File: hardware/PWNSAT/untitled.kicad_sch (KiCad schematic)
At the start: 54 parts, among them J1 Conn_01x03, J2 Conn_01x04_Pin, SW1 SW_Push, SW2 SW_Push, U2 W25N02KVZEIR, Y1 Crystal, Y2 24MHz

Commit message: feat(Hw):Update_Battery_Sch_And_Sensors_And_PWNCube
pending_Outputs_connectors
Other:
- company: (none) -> ElectronicCats
- title: (none) -> PWNCube
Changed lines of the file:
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@@
 	(generator_version "9.0")
 	(paper "A3")
+	(title_block
+		(title "PWNCube")
+		(date "2026-01-23")
+		(rev "1.0")
+		(company "ElectronicCats")
+		(comment 1 "Edgar Capuchino")
+	)
 	(text "FLASH\n"
 		(exclude_from_sim no)

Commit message: feat(Hw):floorplans_updated
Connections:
- net R1_SCK: now reaches U1.38 (EMMC_D5/SPI1_CLK_M0/UART1_RX_M2/I2C2_SCL_M1/GPIO4__A7_U)
- net R1_NSS: now reaches U1.40 (EMMC_D4/SPI1_CS0_M0/UART1_TX_M2/I2C2_SDA_M1/GPIO4__A5_U)
- net R1_MOSI: now reaches U1.45 (EMMC_D6/SPI1_MOSI_M0/UART0_TX_M2/I2C0_SCL_M1/GPIO_4_A1_U)
- net R1_MISO: now reaches U1.46 (EMMC_D7/SPI1_MISO_M0/UART0_RX_M2/I2C0_SDA_M1/GPIO_4_A0_U)
- net R1_RST: now reaches U1.83 (VO_LCDC_D1/VI_CIF_D8_M1/PWM10_M1/UART4_RTS__M1/GPIO1_C6_D)
- net R1_BUSY: now reaches U1.84 (VO_LCDC_D0/VI_CIF_D9_M1/PWM11_IR_M1/UART4_CT_S_M1/GPIO1_C7_D)
- net R1_DIO3: now reaches U1.85 (VO_LCDC_CLK/VI_CIF_CLKO_M1/I2C3_SCL_M1/UART5__TX_M1/PWM11_IR_M2/AUD_DSM_N/GPIO1_D3_D)
- net R1_DIO2: now reaches U1.86 (VO_LCDC_VSYNC/VI_CIF_VSYNC_M1/I2C3_SDA_M1/UA_RT5_RX_M1/SPI0_CS1_M0/PWM0_M1/AUD_DSM_P/GPI_O1_D2_D)
- net R1_DIO1: now reaches U1.87 (VO_LCDC_HSYNC/VI_CIF_HREF_M1/PWM10_M2/UART5__CTS_M1/UART3_RX_M1/GPIO1_D1_D)
- net DIO23: now reaches U1.89 (VO_LCDC_DEN/VI_CIF_CLKI_M1/PWM3_IR_M2/UART5__RTS_M1/UART3_TX_M1/GPIO1_D0_D)
- net R1_ANT_SW: now reaches U1.90 (VO_LCDC_D2/VI_CIF_D7_M1/PWM9_M1/UART4_TX_M1/_SDMMC1_D2_M1/GPIO1_C5_D)
- no-connect marks 56 -> 45
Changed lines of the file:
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@@
 	)
 	(no_connect
-		(at 283.21 88.9)
-	)
-	(no_connect
 		(at 287.02 177.8)
 	)
@@
 	)
 	(no_connect
-		(at 283.21 81.28)
-	)
-	(no_connect
 		(at 144.78 127)
 	)
 	(no_connect
-		(at 144.78 142.24)
-	)
-	(no_connect
 		(at 287.02 195.58)
 	)
@@
 	)
 	(no_connect
-		(at 144.78 137.16)
-	)
-	(no_connect
 		(at 287.02 147.32)
 	)
@@
 	)
 	(no_connect
-		(at 283.21 91.44)
-	)
-	(no_connect
 		(at 287.02 142.24)
 	)
@@
 	)
 	(no_connect
-		(at 283.21 83.82)
-	)
-	(no_connect
 		(at 134.62 39.37)
 	)
@@
 	)
 	(no_connect
-		(at 144.78 157.48)
-	)
-	(no_connect
 		(at 287.02 154.94)
 	)
@@
 	)
 	(no_connect
-		(at 283.21 76.2)
-	)
-	(no_connect
 		(at 134.62 95.25)
 	)
@@
 	)
 	(no_connect
-		(at 283.21 73.66)
-	)
-	(no_connect
-		(at 283.21 78.74)
-	)
-	(no_connect
 		(at 283.21 58.42)
 	)
@@
 	)
 	(no_connect
-		(at 144.78 154.94)
-	)
-	(no_connect
 		(at 287.02 165.1)
 	)
@@
 	(wire
 		(pts
+			(xy 271.78 81.28) (xy 283.21 81.28)
+		)
+		(stroke
+			(width 0)
+			(type default)
+		)
+	)
+	(wire
+		(pts
 			(xy 214.63 256.54) (xy 212.09 256.54)
 		)
@@
 	(wire
 		(pts
-			(xy 127 134.62) (xy 144.78 134.62)
+			(xy 120.65 134.62) (xy 144.78 134.62)
 		)
 		(stroke
@@
 	(wire
 		(pts
+			(xy 271.78 91.44) (xy 283.21 91.44)
+		)
+		(stroke
+			(width 0)
+			(type default)
+		)
+	)
+	(wire
+		(pts
 			(xy 57.15 80.01) (xy 57.15 82.55)
 		)
@@
 	(wire
 		(pts
-			(xy 127 138.43) (xy 127 134.62)
+			(xy 120.65 137.16) (xy 120.65 134.62)
 		)
 		(stroke
@@
 	(wire
 		(pts
+			(xy 271.78 83.82) (xy 283.21 83.82)
+		)
+		(stroke
+			(width 0)
+			(type default)
+		)
+	)
+	(wire
+		(pts
 			(xy 74.93 82.55) (xy 74.93 80.01)
 		)
@@
 	(wire
 		(pts
+			(xy 129.54 154.94) (xy 144.78 154.94)
+		)
+		(stroke
+			(width 0)
+			(type default)
+		)
+	)
+	(wire
+		(pts
 			(xy 44.45 54.61) (xy 44.45 58.42)
 		)
@@
 	(wire
 		(pts
+			(xy 129.54 157.48) (xy 144.78 157.48)
+		)
+		(stroke
+			(width 0)
+			(type default)
+		)
+	)
+	(wire
+		(pts
 			(xy 50.8 71.12) (xy 50.8 73.66)
 		)
@@
 	(wire
 		(pts
+			(xy 271.78 76.2) (xy 283.21 76.2)
+		)
+		(stroke
+			(width 0)
+			(type default)
+		)
+	)
+	(wire
+		(pts
 			(xy 274.32 162.56) (xy 287.02 162.56)
 		)
@@
 	(wire
 		(pts
+			(xy 129.54 137.16) (xy 144.78 137.16)
+		)
+		(stroke
+			(width 0)
+			(type default)
+		)
+	)
+	(wire
+		(pts
+			(xy 271.78 88.9) (xy 283.21 88.9)
+		)
+		(stroke
+			(width 0)
+			(type default)
+		)
+	)
+	(wire
+		(pts
 			(xy 248.92 271.78) (xy 238.76 271.78)
 		)
@@
 	(wire
 		(pts
+			(xy 271.78 78.74) (xy 283.21 78.74)
+		)
+		(stroke
+			(width 0)
+			(type default)
+		)
+	)
+	(wire
+		(pts
 			(xy 33.02 110.49) (xy 33.02 113.03)
 		)
@@
 	(wire
 		(pts
+			(xy 271.78 73.66) (xy 283.21 73.66)
+		)
+		(stroke
+			(width 0)
+			(type default)
+		)
+	)
+	(wire
+		(pts
 			(xy 119.38 80.01) (xy 134.62 80.01)
 		)
@@
 	(wire
 		(pts
+			(xy 129.54 142.24) (xy 144.78 142.24)
+		)
+		(stroke
+			(width 0)
+			(type default)
+		)
+	)
+	(wire
+		(pts
 			(xy 22.86 100.33) (xy 24.13 100.33)
 		)
@@
 		)
 	)
+	(hierarchical_label "R1_BUSY"
+		(shape input)
+		(at 271.78 76.2 180)
+		(effects
+			(font
+				(size 1.27 1.27)
+			)
+			(justify right)
+		)
+	)
 	(hierarchical_label "DIO2"
 		(shape input)
@@
 		)
 	)
+	(hierarchical_label "R1_MOSI"
+		(shape input)
+		(at 129.54 154.94 180)
+		(effects
+			(font
+				(size 1.27 1.27)
+			)
+			(justify right)
+		)
+	)
 	(hierarchical_label "INT2"
 		(shape output)
@@
 		)
 	)
+	(hierarchical_label "R1_ANT_SW"
+		(shape input)
+		(at 271.78 91.44 180)
+		(effects
+			(font
+				(size 1.27 1.27)
+			)
+			(justify right)
+		)
+	)
 	(hierarchical_label "R0_MOSI"
 		(shape input)
@@
 		)
 	)
+	(hierarchical_label "R1_DIO3"
+		(shape input)
+		(at 271.78 78.74 180)
+		(effects
+			(font
+				(size 1.27 1.27)
+			)
+			(justify right)
+		)
+	)
 	(hierarchical_label "v_0.9v"
 		(shape input)
@@
 		)
 	)
+	(hierarchical_label "R1_NSS"
+		(shape input)
+		(at 129.54 142.24 180)
+		(effects
+			(font
+				(size 1.27 1.27)
+			)
+			(justify right)
+		)
+	)
 	(hierarchical_label "v_0.9v"
 		(shape input)
@@
 		)
 	)
+	(hierarchical_label "R1_MISO"
+		(shape input)
+		(at 129.54 157.48 180)
+		(effects
+			(font
+				(size 1.27 1.27)
+			)
+			(justify right)
+		)
+	)
 	(hierarchical_label "v_3v3"
 		(shape input)
@@
 		)
 	)
+	(hierarchical_label "R1_DIO2"
+		(shape input)
+		(at 271.78 81.28 180)
+		(effects
+			(font
+				(size 1.27 1.27)
+			)
+			(justify right)
+		)
+	)
 	(hierarchical_label "INT1"
 		(shape output)
@@
 		)
 	)
+	(hierarchical_label "R1_DIO1"
+		(shape input)
+		(at 271.78 83.82 180)
+		(effects
+			(font
+				(size 1.27 1.27)
+			)
+			(justify right)
+		)
+	)
 	(hierarchical_label "VCC_DDR"
 		(shape input)
@@
 		)
 	)
+	(hierarchical_label "R1_SCK"
+		(shape input)
+		(at 129.54 137.16 180)
+		(effects
+			(font
+				(size 1.27 1.27)
+			)
+			(justify right)
+		)
+	)
 	(hierarchical_label "v_0.9v"
 		(shape input)
@@
 		)
 	)
+	(hierarchical_label "R1_RST"
+		(shape input)
+		(at 271.78 73.66 180)
+		(effects
+			(font
+				(size 1.27 1.27)
+			)
+			(justify right)
+		)
+	)
 	(hierarchical_label "v_3v3"
 		(shape input)
@@
 		)
 	)
+	(hierarchical_label "DIO23"
+		(shape input)
+		(at 271.78 88.9 180)
+		(effects
+			(font
+				(size 1.27 1.27)
+			)
+			(justify right)
+		)
+	)
 	(hierarchical_label "v_1.8v"
 		(shape input)
@@
 	(symbol
 		(lib_id "power:GND")
-		(at 127 138.43 0)
+		(at 120.65 137.16 0)
 		(unit 1)
 		(exclude_from_sim no)
@@
 		(dnp no)
 		(property "Reference" "#PWR016"
-			(at 127 144.78 0)
+			(at 120.65 143.51 0)
 			(effects
 				(font
@@
 		)
 		(property "Value" "GND"
-			(at 123.952 138.684 0)
+			(at 117.602 137.414 0)
 			(effects
 				(font
@@
 		)
 		(property "Footprint" ""
-			(at 127 138.43 0)
+			(at 120.65 137.16 0)
 			(effects
 				(font
@@
 		)
 		(property "Datasheet" ""
-			(at 127 138.43 0)
+			(at 120.65 137.16 0)
 			(effects
 				(font
@@
 		)
 		(property "Description" "Power symbol creates a global label with name \"GND\" , ground"
-			(at 127 138.43 0)
+			(at 120.65 137.16 0)
 			(effects
 				(font

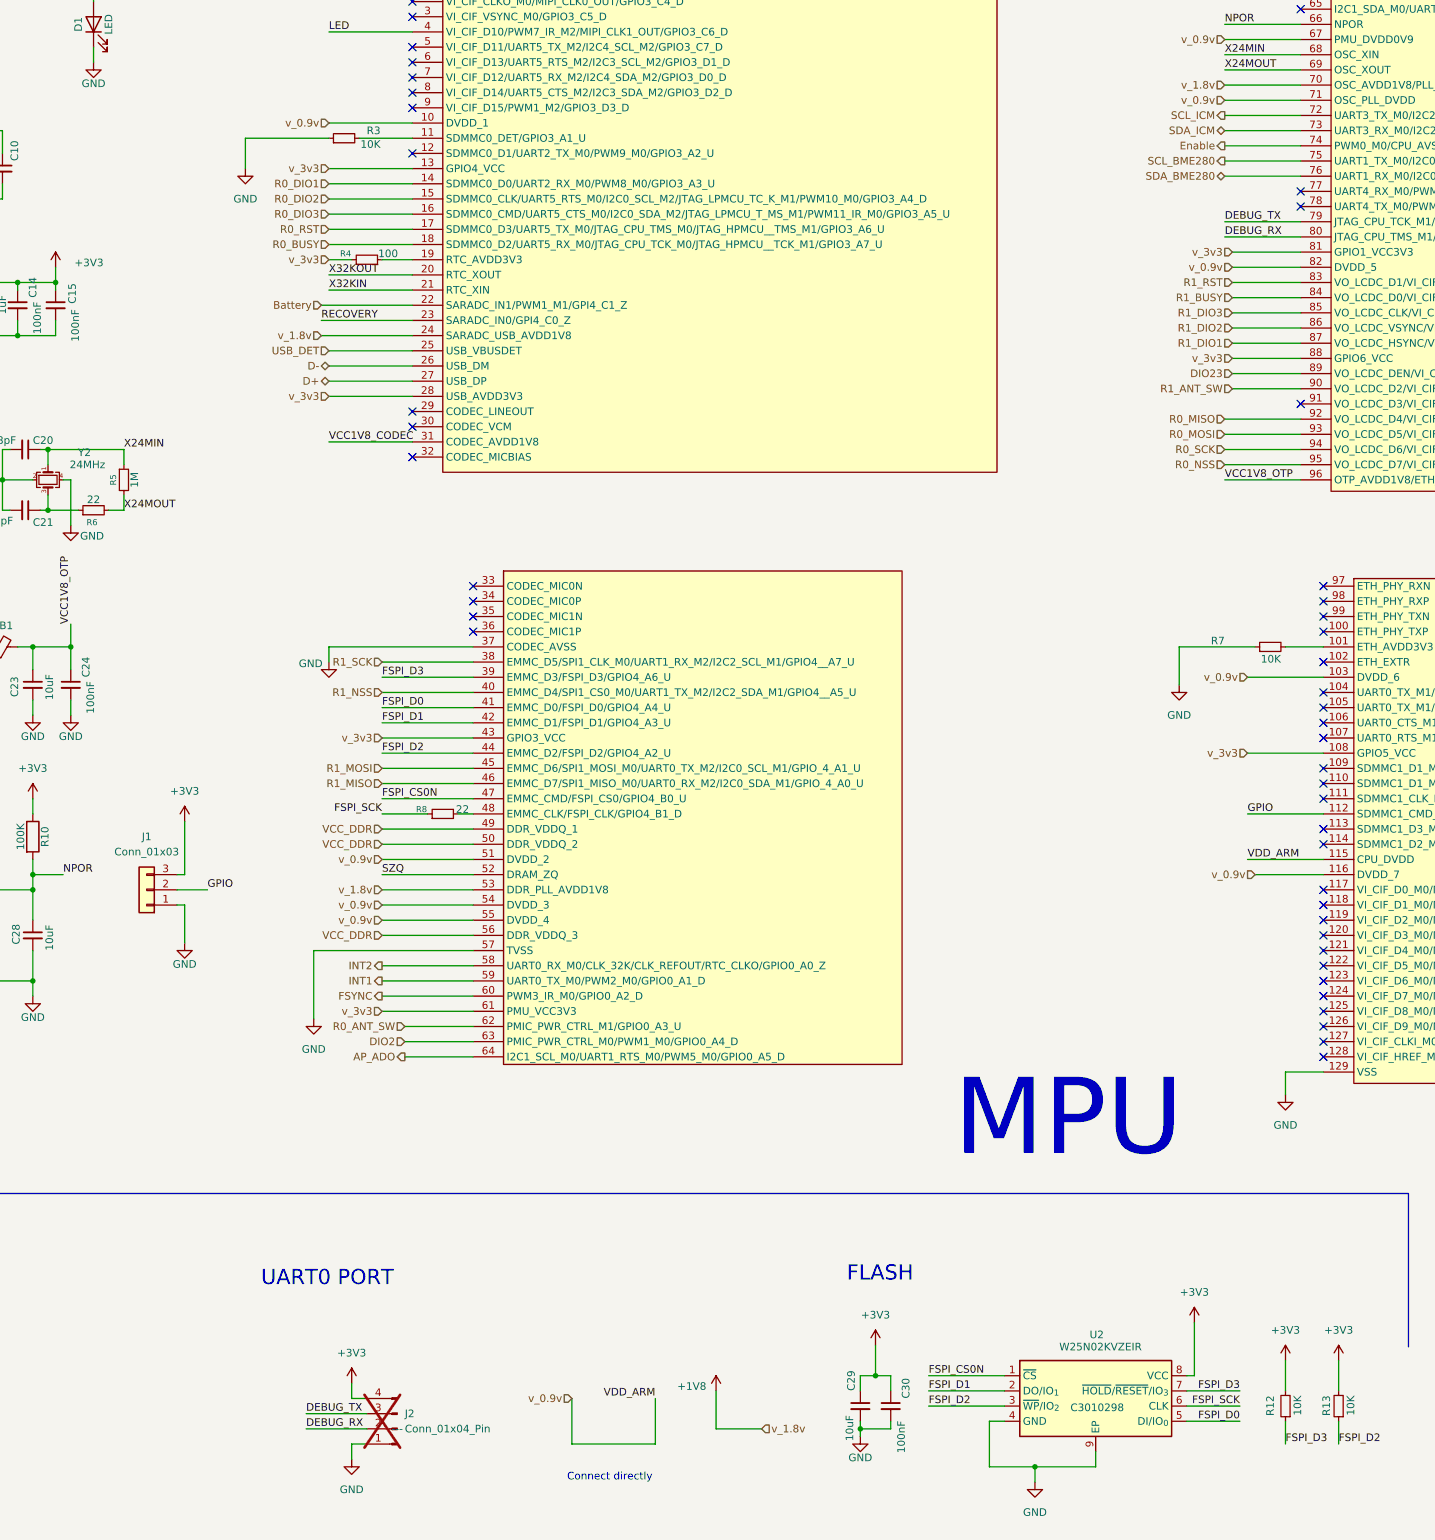
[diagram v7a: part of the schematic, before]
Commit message: feat(Hw):Boards_Updated
Pending_Sensors_Board
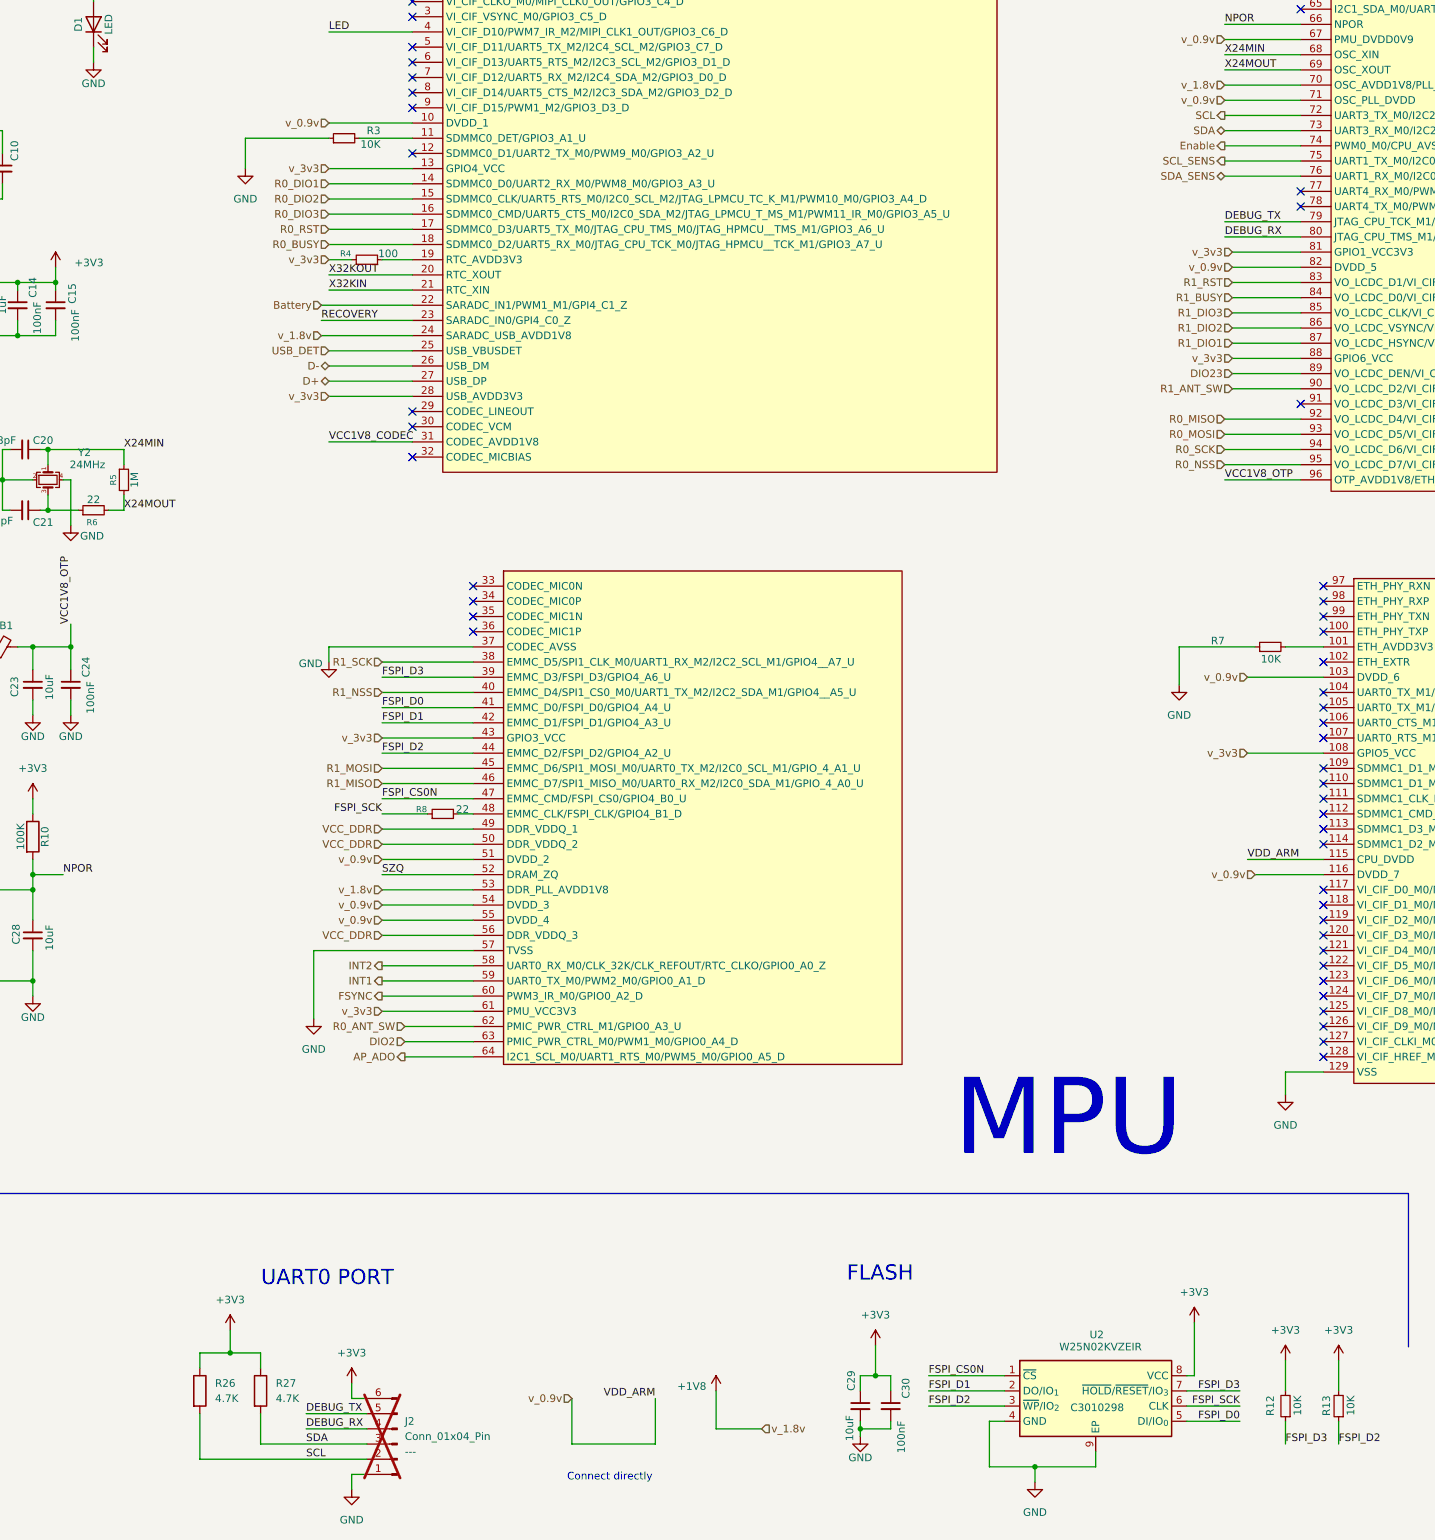
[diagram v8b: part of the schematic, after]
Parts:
- removed J1: Conn_01x03, Connector_PinHeader_2.54mm:PinHeader_1x03_P2.54mm_Vertical, symbol Connector_Generic:Conn_01x03
- added R26, R27: 4.7K, Resistor_SMD:R_0402_1005Metric_Pad0.72x0.64mm_HandSolder, symbol Device:R
- J2: footprint Connector_PinHeader_2.54mm:PinHeader_1x04_P2.54mm_Vertical -> Connector_PinHeader_2.54mm:PinHeader_1x06_P2.54mm_Vertical; symbol Connector:Conn_01x04_Pin -> Connector:Conn_01x06_Pin
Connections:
- net +3V3: now also J2.6 (Pin_6), R26.1, R27.1; no longer J2.4 (Pin_4)
- net DEBUG_RX: now also J2.4 (Pin_4); no longer J2.2 (Pin_2)
- net DEBUG_TX: now also J2.5 (Pin_5); no longer J2.3 (Pin_3)
- net GPIO: no longer names the net of U1.112 (SDMMC1_CMD_M0/I2S0_SDO3_SDI1/VO_LCDC_D11/GP_IO2_A3_D)
- net SCL_BME280 renamed SCL_SENS
- net SCL_ICM renamed SCL
- net SCL: now also J2.2 (Pin_2), R26.2
- net SDA_BME280 renamed SDA_SENS
- net SDA_ICM renamed SDA
- net SDA: now also J2.3 (Pin_3), R27.2
- no-connect marks 45 -> 46
